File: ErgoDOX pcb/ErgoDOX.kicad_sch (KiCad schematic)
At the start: 64 parts

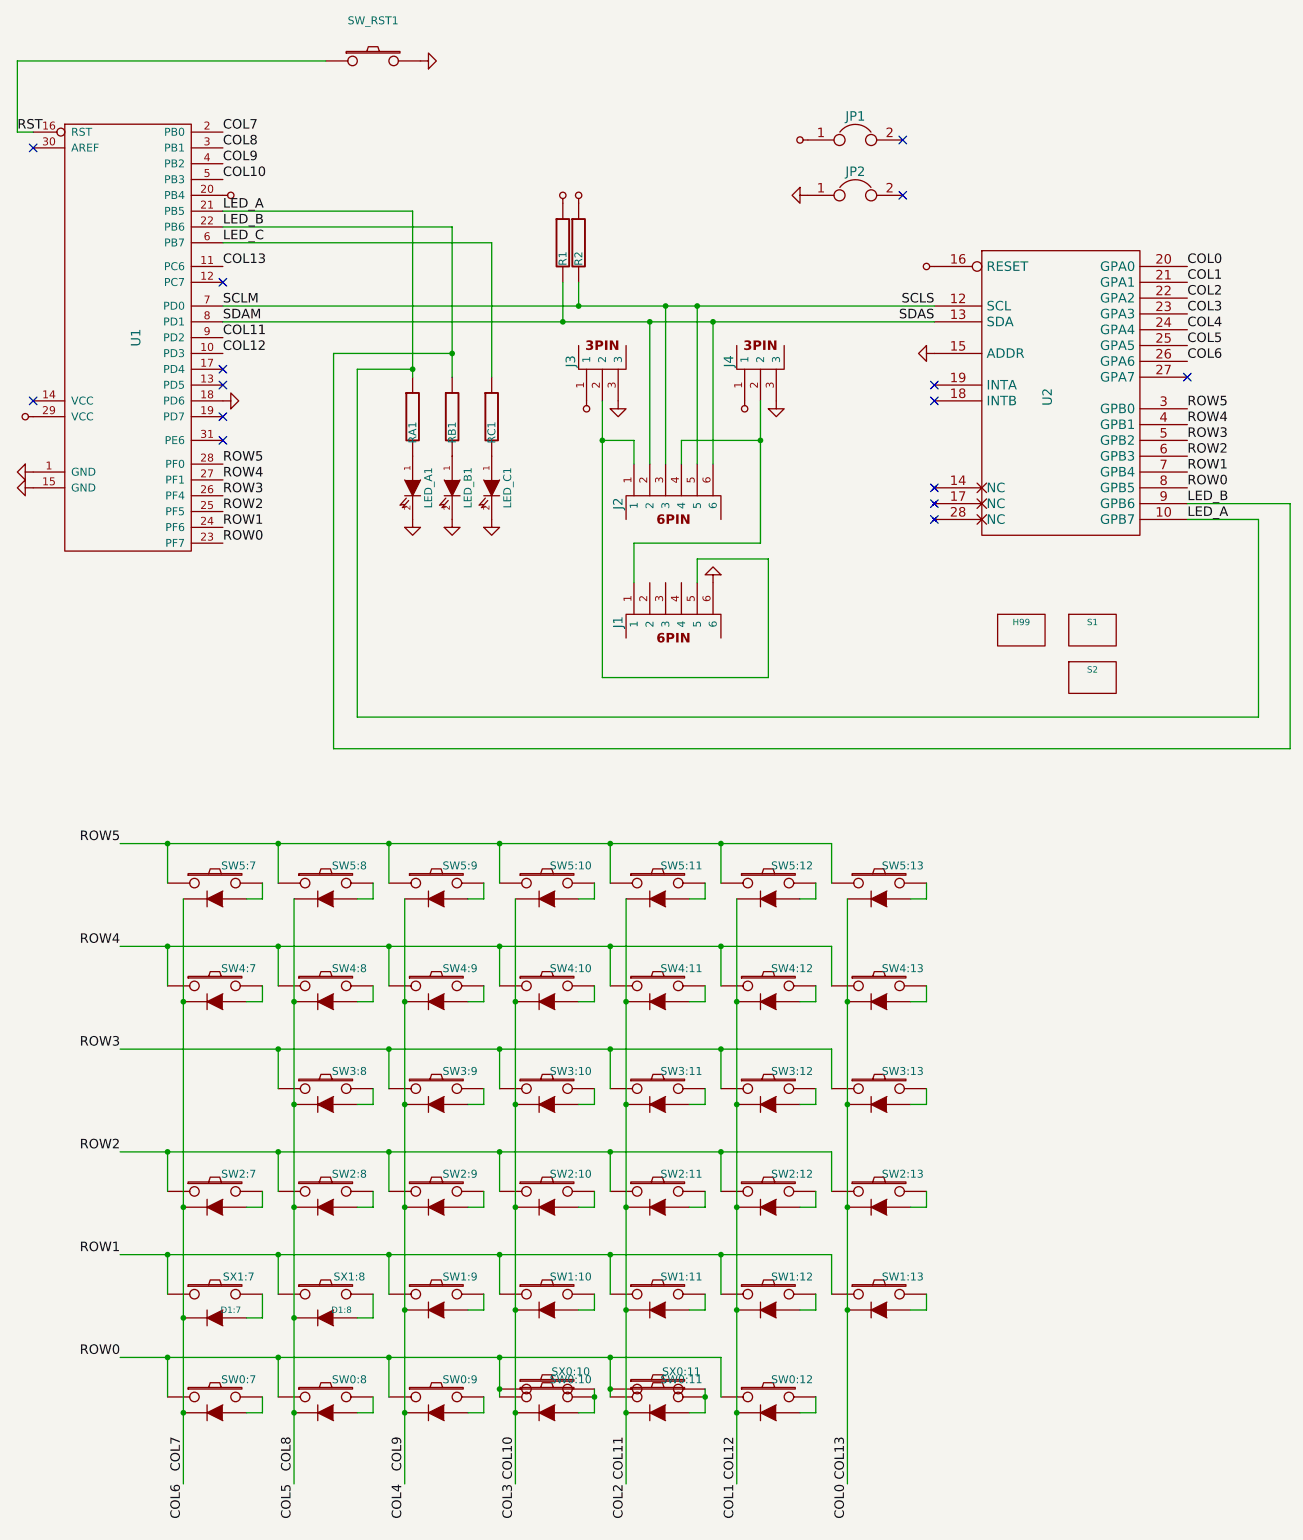
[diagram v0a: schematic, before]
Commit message: add encoder switch
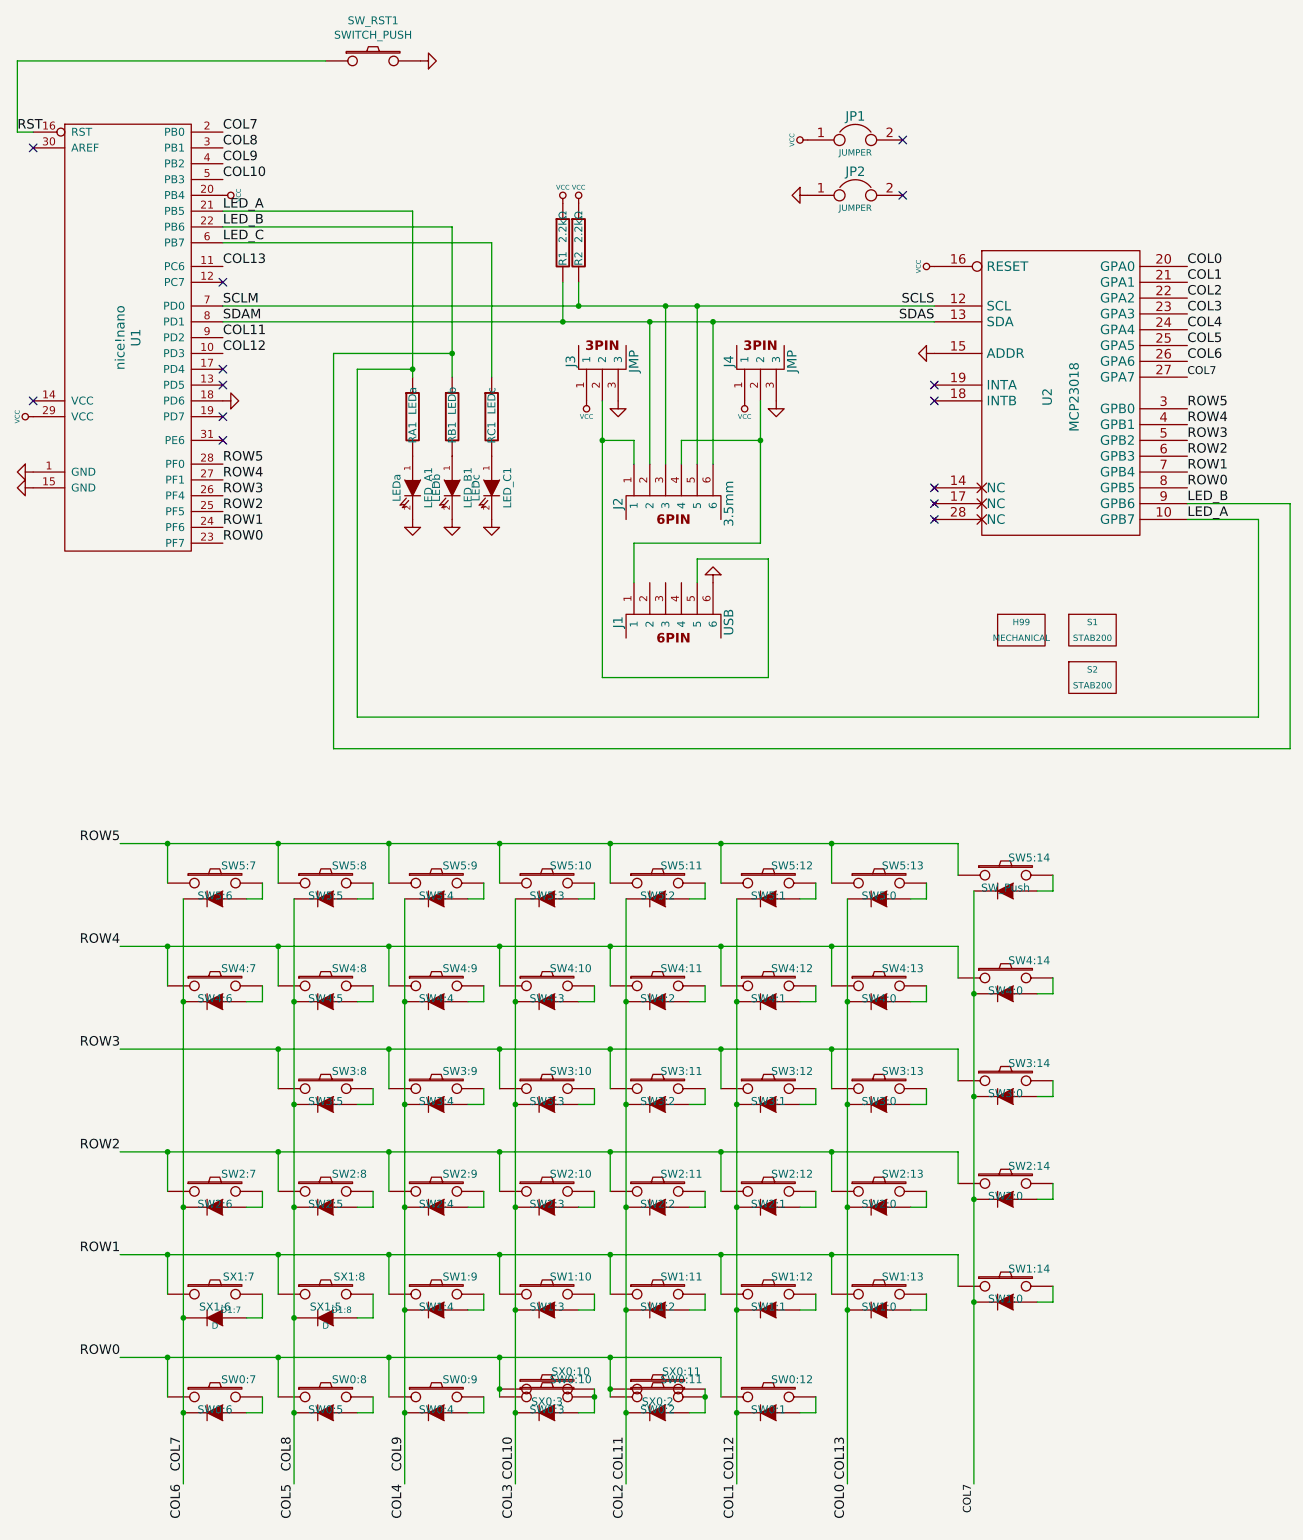
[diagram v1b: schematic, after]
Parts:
- added SW1:14: SW1:0, symbol component:SWITCH_DIODE
- added SW2:14: SW2:0, symbol component:SWITCH_DIODE
- added SW3:14: SW3:0, symbol component:SWITCH_DIODE
- added SW4:14: SW4:0, symbol component:SWITCH_DIODE
- added SW5:14: SW_Push, ErgoDOX pcb:Choc_Hotswap, symbol component:SWITCH_DIODE
- D1:7, D1:8: value (none) -> D
- H99: value (none) -> MECHANICAL
- J1: value (none) -> USB
- J2: value (none) -> 3.5mm
- J3, J4: value (none) -> JMP
- JP1, JP2: value (none) -> JUMPER
- LED_A1, RA1: value (none) -> LEDa
- LED_B1, RB1: value (none) -> LEDb
- LED_C1, RC1: value (none) -> LEDc
- R1, R2: value (none) -> 2.2kΩ
- S1, S2: value (none) -> STAB200
- SW0:10: value (none) -> SW0:3; footprint (none) -> ErgoDOX pcb:Choc_Hotswap
- SW0:11: value (none) -> SW0:2; footprint (none) -> ErgoDOX pcb:Choc_Hotswap
- SW0:12: value (none) -> SW0:1; footprint (none) -> ErgoDOX pcb:Choc_Hotswap
- SW0:7: value (none) -> SW0:6; footprint (none) -> ErgoDOX pcb:Choc_Hotswap
- SW0:8: value (none) -> SW0:5; footprint (none) -> ErgoDOX pcb:Choc_Hotswap
- SW0:9: value (none) -> SW0:4; footprint (none) -> ErgoDOX pcb:Choc_Hotswap
- SW1:10: value (none) -> SW1:3; footprint (none) -> ErgoDOX pcb:Choc_Hotswap
- SW1:11: value (none) -> SW1:2; footprint (none) -> ErgoDOX pcb:Choc_Hotswap
- SW1:12: value (none) -> SW1:1; footprint (none) -> ErgoDOX pcb:Choc_Hotswap
- SW1:13: value (none) -> SW1:0; footprint (none) -> ErgoDOX pcb:Choc_Hotswap_1u+1.5u
- SW1:9: value (none) -> SW1:4; footprint (none) -> ErgoDOX pcb:Choc_Hotswap
- SW2:10: value (none) -> SW2:3; footprint (none) -> ErgoDOX pcb:Choc_Hotswap
- SW2:11: value (none) -> SW2:2; footprint (none) -> ErgoDOX pcb:Choc_Hotswap
- SW2:12: value (none) -> SW2:1; footprint (none) -> ErgoDOX pcb:Choc_Hotswap
- SW2:13: value (none) -> SW2:0; footprint (none) -> ErgoDOX pcb:Choc_Hotswap_1u+1.5u
- SW2:7: value (none) -> SW2:6; footprint (none) -> ErgoDOX pcb:Choc_Hotswap
- SW2:8: value (none) -> SW2:5; footprint (none) -> ErgoDOX pcb:Choc_Hotswap
- SW2:9: value (none) -> SW2:4; footprint (none) -> ErgoDOX pcb:Choc_Hotswap
- SW3:10: value (none) -> SW3:3; footprint (none) -> ErgoDOX pcb:Choc_Hotswap
- SW3:11: value (none) -> SW3:2; footprint (none) -> ErgoDOX pcb:Choc_Hotswap
- SW3:12: value (none) -> SW3:1; footprint (none) -> ErgoDOX pcb:Choc_Hotswap
- SW3:13: value (none) -> SW3:0; footprint (none) -> ErgoDOX pcb:Choc_Hotswap_1u+1.5u
- SW3:8: value (none) -> SW3:5; footprint (none) -> ErgoDOX pcb:Choc_Hotswap
- SW3:9: value (none) -> SW3:4; footprint (none) -> ErgoDOX pcb:Choc_Hotswap
- SW4:10: value (none) -> SW4:3; footprint (none) -> ErgoDOX pcb:Choc_Hotswap
- SW4:11: value (none) -> SW4:2; footprint (none) -> ErgoDOX pcb:Choc_Hotswap
- SW4:12: value (none) -> SW4:1; footprint (none) -> ErgoDOX pcb:Choc_Hotswap
- SW4:13: value (none) -> SW4:0; footprint (none) -> ErgoDOX pcb:Choc_Hotswap_1u+1.5u
- SW4:7: value (none) -> SW4:6; footprint (none) -> ErgoDOX pcb:Choc_Hotswap
- SW4:8: value (none) -> SW4:5; footprint (none) -> ErgoDOX pcb:Choc_Hotswap
- SW4:9: value (none) -> SW4:4; footprint (none) -> ErgoDOX pcb:Choc_Hotswap
- SW5:10: value (none) -> SW5:3; footprint (none) -> ErgoDOX pcb:Choc_Hotswap
- SW5:11: value (none) -> SW5:2; footprint (none) -> ErgoDOX pcb:Choc_Hotswap
- SW5:12: value (none) -> SW5:1; footprint (none) -> ErgoDOX pcb:Choc_Hotswap
- SW5:13: value (none) -> SW5:0; footprint (none) -> ErgoDOX pcb:Choc_Hotswap_1u+1.5u
- SW5:7: value (none) -> SW5:6; footprint (none) -> ErgoDOX pcb:Choc_Hotswap
- SW5:8: value (none) -> SW5:5; footprint (none) -> ErgoDOX pcb:Choc_Hotswap
- SW5:9: value (none) -> SW5:4; footprint (none) -> ErgoDOX pcb:Choc_Hotswap
- SW_RST1: value (none) -> SWITCH_PUSH; footprint (none) -> Buttons_Switches_SMD:SW_SPST_B3U-1000P
- SX0:10: value (none) -> SX0:3
- SX0:11: value (none) -> SX0:2
- SX1:7: value (none) -> SX1:6
- SX1:8: value (none) -> SX1:5
- U1: value (none) -> nice!nano; footprint (none) -> ErgoDOX pcb:nicenano
- U2: value (none) -> MCP23018
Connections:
- net COL6: now also U2.27 (GPA7), SW1:14.4 (K), SW2:14.4 (K), SW3:14.4 (K), SW4:14.4 (K), SW5:14.4 (K)
- net GND: now also SW1:14.0 (GND), SW2:14.0 (GND), SW3:14.0 (GND), SW4:14.0 (GND), SW5:14.0 (GND)
- net ROW1: now also SW1:14.1
- net ROW2: now also SW2:14.1
- net ROW3: now also SW3:14.1
- net ROW4: now also SW4:14.1
- net ROW5: now also SW5:14.1
- new net: SW2:14.2, SW2:14.3 (A)
- new net: SW4:14.2, SW4:14.3 (A)
- new net: SW1:14.2, SW1:14.3 (A)
- new net: SW3:14.2, SW3:14.3 (A)
- new net: SW5:14.2, SW5:14.3 (A)
- no-connect marks 15 -> 14
